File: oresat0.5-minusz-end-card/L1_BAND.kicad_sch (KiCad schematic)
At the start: 1 part

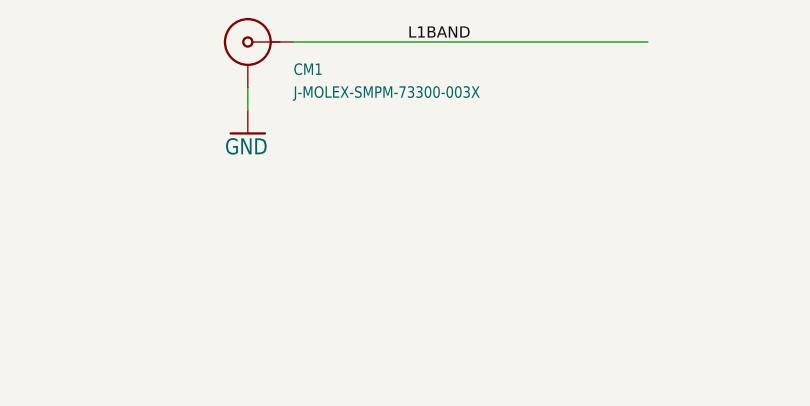
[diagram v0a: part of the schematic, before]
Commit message: Updated -Z end card and replaced eagle imported libraries with kicad libraries
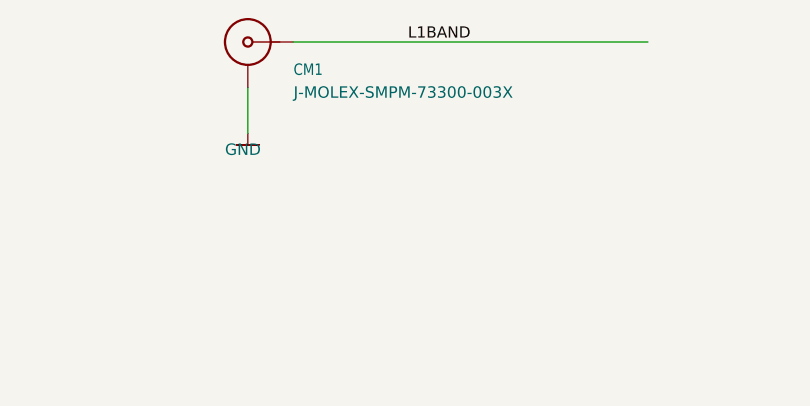
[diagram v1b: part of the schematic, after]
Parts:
- CM1: footprint oresat-footprints:J-MOLEX-SMPM-073300-003X -> oresat-connectors:J-MOLEX-SMPM-073300-003X; symbol OreSat-j-molex-smpm-73300-003x:J-MOLEX-SMPM-73300-003X -> oresat-connectors:J-MOLEX-SMPM-73300-003X
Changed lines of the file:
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@@
     (stroke (width 0) (type default) (color 0 0 0 0))
   )
-  (wire (pts (xy 57.15 139.7) (xy 57.15 137.16))
+  (wire (pts (xy 57.15 137.16) (xy 57.15 142.24))
     (stroke (width 0) (type default) (color 0 0 0 0))
   )
@@
     (effects (font (size 1.2446 1.2446)) (justify left bottom))
   )
-  (symbol (lib_id "OreSat-j-molex-smpm-73300-003x:J-MOLEX-SMPM-73300-003X") (at 57.15 132.08 0) (unit 1)
+  (symbol (lib_id "oresat-connectors:J-MOLEX-SMPM-73300-003X") (at 57.15 132.08 0) (unit 1)
     (in_bom yes) (on_board yes)
     (property "Reference" "CM1" (id 0) (at 62.23 135.89 0)
@@
     )
     (property "Value" "J-MOLEX-SMPM-73300-003X" (id 1) (at 62.23 138.43 0)
-      (effects (font (size 1.27 1.0795)) (justify left bottom))
+      (effects (font (size 1.27 1.27)) (justify left bottom))
     )
-    (property "Footprint" "oresat-footprints:J-MOLEX-SMPM-073300-003X" (id 2) (at 57.15 132.08 0)
+    (property "Footprint" "oresat-connectors:J-MOLEX-SMPM-073300-003X" (id 2) (at 57.15 132.08 0)
       (effects (font (size 1.27 1.27)) hide)
     )
@@
     (pin "RF")
   )
-  (symbol (lib_id "plusz-end-card-with-turnstile-eagle-import:GND") (at 57.15 142.24 0) (unit 1)
+  (symbol (lib_id "oresat-power:GND") (at 57.15 142.24 0) (unit 1)
     (in_bom yes) (on_board yes)
     (property "Reference" "#GND012" (id 0) (at 57.15 142.24 0)
@@
     )
     (property "Value" "GND" (id 1) (at 54.61 144.78 0)
-      (effects (font (size 1.778 1.5113)) (justify left bottom))
+      (effects (font (size 1.27 1.27)) (justify left bottom))
     )
     (property "Footprint" "plusz-end-card-with-turnstile:" (id 2) (at 57.15 142.24 0)

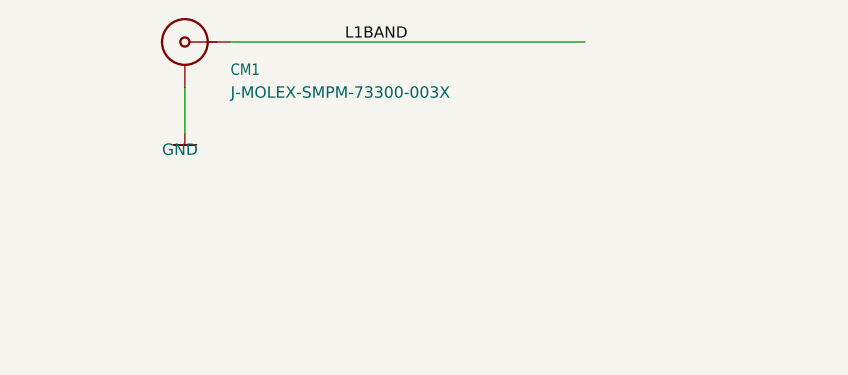
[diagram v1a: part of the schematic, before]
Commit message: -Z end card design review changes, and added antenna feeds
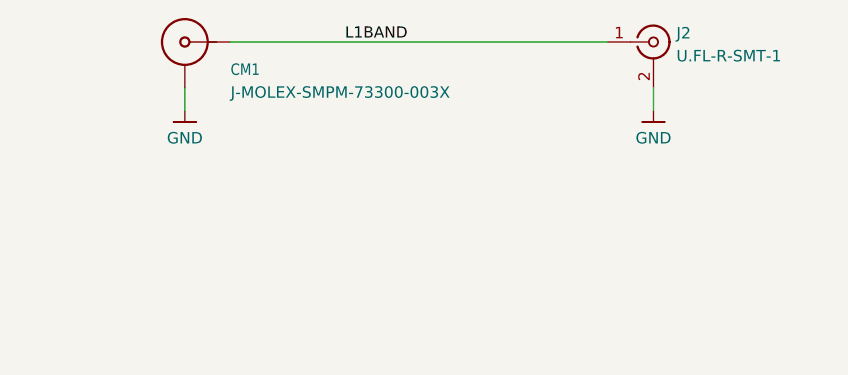
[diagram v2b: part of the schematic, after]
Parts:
- added J2: U.FL-R-SMT-1, Connector_Coaxial:U.FL_Hirose_U.FL-R-SMT-1_Vertical, symbol Connector:Conn_Coaxial
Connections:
- net GND: now also J2.2 (Ext)
- net L1BAND: now also J2.1 (In)
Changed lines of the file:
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@@
     (rev "1.0")
   )
-  (wire (pts (xy 62.23 132.08) (xy 101.6 132.08))
+  (wire (pts (xy 109.22 137.16) (xy 109.22 139.7))
     (stroke (width 0) (type default) (color 0 0 0 0))
   )
-  (wire (pts (xy 57.15 137.16) (xy 57.15 142.24))
+  (wire (pts (xy 62.23 132.08) (xy 104.14 132.08))
+    (stroke (width 0) (type default) (color 0 0 0 0))
+  )
+  (wire (pts (xy 57.15 137.16) (xy 57.15 139.7))
     (stroke (width 0) (type default) (color 0 0 0 0))
   )
@@
   (label "L1BAND" (at 74.93 132.08 0)
     (effects (font (size 1.2446 1.2446)) (justify left bottom))
+  )
+  (symbol (lib_id "Connector:Conn_Coaxial") (at 109.22 132.08 0) (unit 1)
+    (in_bom yes) (on_board yes) (fields_autoplaced)
+    (property "Reference" "J2" (id 0) (at 111.76 131.1031 0)
+      (effects (font (size 1.27 1.27)) (justify left))
+    )
+    (property "Value" "U.FL-R-SMT-1" (id 1) (at 111.76 133.6431 0)
+      (effects (font (size 1.27 1.27)) (justify left))
+    )
+    (property "Footprint" "Connector_Coaxial:U.FL_Hirose_U.FL-R-SMT-1_Vertical" (id 2) (at 109.22 132.08 0)
+      (effects (font (size 1.27 1.27)) hide)
+    )
+    (property "Datasheet" " ~" (id 3) (at 109.22 132.08 0)
+      (effects (font (size 1.27 1.27)) hide)
+    )
+    (pin "1")
+    (pin "2")
+  )
+  (symbol (lib_id "oresat-power:GND") (at 109.22 139.7 0) (unit 1)
+    (in_bom yes) (on_board yes)
+    (property "Reference" "#GND03" (id 0) (at 109.22 139.7 0)
+      (effects (font (size 1.27 1.27)) hide)
+    )
+    (property "Value" "GND" (id 1) (at 109.22 143.51 0)
+      (effects (font (size 1.27 1.27)) (justify bottom))
+    )
+    (property "Footprint" "plusz-end-card-with-turnstile:" (id 2) (at 109.22 139.7 0)
+      (effects (font (size 1.27 1.27)) hide)
+    )
+    (property "Datasheet" "" (id 3) (at 109.22 139.7 0)
+      (effects (font (size 1.27 1.27)) hide)
+    )
+    (pin "1")
   )
   (symbol (lib_id "oresat-connectors:J-MOLEX-SMPM-73300-003X") (at 57.15 132.08 0) (unit 1)
@@
     (pin "RF")
   )
-  (symbol (lib_id "oresat-power:GND") (at 57.15 142.24 0) (unit 1)
+  (symbol (lib_id "oresat-power:GND") (at 57.15 139.7 0) (unit 1)
     (in_bom yes) (on_board yes)
-    (property "Reference" "#GND012" (id 0) (at 57.15 142.24 0)
+    (property "Reference" "#GND012" (id 0) (at 57.15 139.7 0)
       (effects (font (size 1.27 1.27)) hide)
     )
-    (property "Value" "GND" (id 1) (at 54.61 144.78 0)
-      (effects (font (size 1.27 1.27)) (justify left bottom))
+    (property "Value" "GND" (id 1) (at 57.15 143.51 0)
+      (effects (font (size 1.27 1.27)) (justify bottom))
     )
-    (property "Footprint" "plusz-end-card-with-turnstile:" (id 2) (at 57.15 142.24 0)
+    (property "Footprint" "plusz-end-card-with-turnstile:" (id 2) (at 57.15 139.7 0)
       (effects (font (size 1.27 1.27)) hide)
     )
-    (property "Datasheet" "" (id 3) (at 57.15 142.24 0)
+    (property "Datasheet" "" (id 3) (at 57.15 139.7 0)
       (effects (font (size 1.27 1.27)) hide)
     )

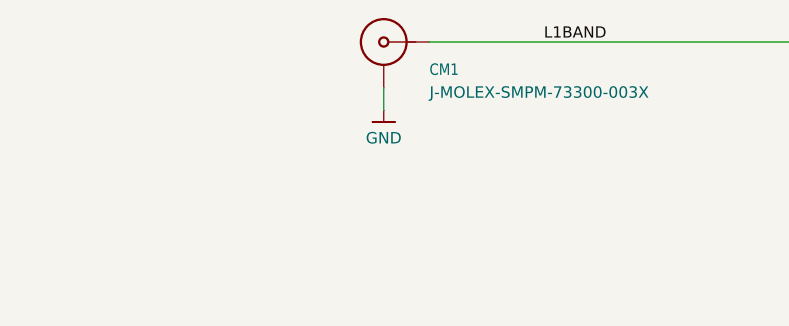
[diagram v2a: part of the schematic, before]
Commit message: Updated OreSat 0.5 end card board outlines and mounting holes, and fixed KiCad library warnings
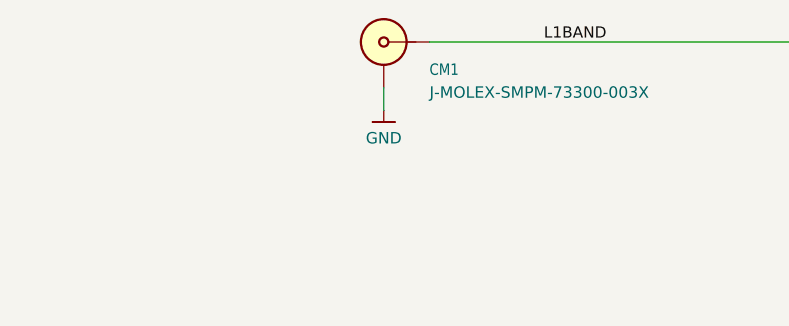
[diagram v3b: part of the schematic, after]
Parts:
- CM1: footprint oresat-connectors:J-MOLEX-SMPM-073300-003X -> oresat-connectors:J-MOLEX-SMPM-073300-002X; symbol oresat-connectors:J-MOLEX-SMPM-73300-003X -> oresat-connectors:J-MOLEX-SMPM-73300-002X
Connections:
- net GND: now also CM1.SHLD; no longer CM1.GND (SHIELD3)
- net L1BAND: now also CM1.SIG; no longer CM1.RF (CENTER)
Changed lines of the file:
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@@
-(kicad_sch (version 20211123) (generator eeschema)
+(kicad_sch (version 20230121) (generator eeschema)
   (paper "USLedger")
   (title_block
@@
   )
   (wire (pts (xy 109.22 137.16) (xy 109.22 139.7))
-    (stroke (width 0) (type default) (color 0 0 0 0))
+    (stroke (width 0) (type default))
   )
   (wire (pts (xy 62.23 132.08) (xy 104.14 132.08))
-    (stroke (width 0) (type default) (color 0 0 0 0))
+    (stroke (width 0) (type default))
   )
   (wire (pts (xy 57.15 137.16) (xy 57.15 139.7))
-    (stroke (width 0) (type default) (color 0 0 0 0))
+    (stroke (width 0) (type default))
   )
-  (text "L1 BAND Feed System (1.575 GHz)" (at 16.51 247.65 180)
+  (text "L1 BAND Feed System (1.575 GHz)" (at 16.51 247.65 0)
     (effects (font (size 4.064 3.4544)) (justify left bottom))
   )
-  (label "L1BAND" (at 74.93 132.08 0)
+  (label "L1BAND" (at 74.93 132.08 0) (fields_autoplaced)
     (effects (font (size 1.2446 1.2446)) (justify left bottom))
   )
   (symbol (lib_id "Connector:Conn_Coaxial") (at 109.22 132.08 0) (unit 1)
-    (in_bom yes) (on_board yes) (fields_autoplaced)
-    (property "Reference" "J2" (id 0) (at 111.76 131.1031 0)
+    (in_bom yes) (on_board yes) (dnp no) (fields_autoplaced)
+    (property "Reference" "J2" (at 111.76 131.1031 0)
       (effects (font (size 1.27 1.27)) (justify left))
     )
-    (property "Value" "U.FL-R-SMT-1" (id 1) (at 111.76 133.6431 0)
+    (property "Value" "U.FL-R-SMT-1" (at 111.76 133.6431 0)
       (effects (font (size 1.27 1.27)) (justify left))
     )
-    (property "Footprint" "Connector_Coaxial:U.FL_Hirose_U.FL-R-SMT-1_Vertical" (id 2) (at 109.22 132.08 0)
+    (property "Footprint" "Connector_Coaxial:U.FL_Hirose_U.FL-R-SMT-1_Vertical" (at 109.22 132.08 0)
       (effects (font (size 1.27 1.27)) hide)
     )
-    (property "Datasheet" " ~" (id 3) (at 109.22 132.08 0)
+    (property "Datasheet" " ~" (at 109.22 132.08 0)
       (effects (font (size 1.27 1.27)) hide)
     )
     (pin "1")
     (pin "2")
+    (instances
+      (project "oresat0.5-minusz-end-card"
+        (path "/f7595184-4323-4ed9-b19e-5e32e3c6e76f/c4a46bba-817b-433a-9d2e-3dc88315141d"
+          (reference "J2") (unit 1)
+        )
+      )
+    )
   )
   (symbol (lib_id "oresat-power:GND") (at 109.22 139.7 0) (unit 1)
-    (in_bom yes) (on_board yes)
-    (property "Reference" "#GND03" (id 0) (at 109.22 139.7 0)
+    (in_bom yes) (on_board yes) (dnp no)
+    (property "Reference" "#GND03" (at 109.22 139.7 0)
       (effects (font (size 1.27 1.27)) hide)
     )
-    (property "Value" "GND" (id 1) (at 109.22 143.51 0)
+    (property "Value" "GND" (at 109.22 143.51 0)
       (effects (font (size 1.27 1.27)) (justify bottom))
     )
-    (property "Footprint" "plusz-end-card-with-turnstile:" (id 2) (at 109.22 139.7 0)
+    (property "Footprint" "plusz-end-card-with-turnstile:" (at 109.22 139.7 0)
       (effects (font (size 1.27 1.27)) hide)
     )
-    (property "Datasheet" "" (id 3) (at 109.22 139.7 0)
+    (property "Datasheet" "" (at 109.22 139.7 0)
       (effects (font (size 1.27 1.27)) hide)
     )
     (pin "1")
+    (instances
+      (project "oresat0.5-minusz-end-card"
+        (path "/f7595184-4323-4ed9-b19e-5e32e3c6e76f/c4a46bba-817b-433a-9d2e-3dc88315141d"
+          (reference "#GND03") (unit 1)
+        )
+      )
+    )
   )
-  (symbol (lib_id "oresat-connectors:J-MOLEX-SMPM-73300-003X") (at 57.15 132.08 0) (unit 1)
-    (in_bom yes) (on_board yes)
-    (property "Reference" "CM1" (id 0) (at 62.23 135.89 0)
+  (symbol (lib_id "oresat-connectors:J-MOLEX-SMPM-73300-002X") (at 57.15 132.08 0) (unit 1)
+    (in_bom yes) (on_board yes) (dnp no)
+    (property "Reference" "CM1" (at 62.23 135.89 0)
       (effects (font (size 1.27 1.0795)) (justify left bottom))
     )
-    (property "Value" "J-MOLEX-SMPM-73300-003X" (id 1) (at 62.23 138.43 0)
+    (property "Value" "J-MOLEX-SMPM-73300-003X" (at 62.23 138.43 0)
       (effects (font (size 1.27 1.27)) (justify left bottom))
     )
-    (property "Footprint" "oresat-connectors:J-MOLEX-SMPM-073300-003X" (id 2) (at 57.15 132.08 0)
+    (property "Footprint" "oresat-connectors:J-MOLEX-SMPM-073300-002X" (at 57.15 125.73 0)
       (effects (font (size 1.27 1.27)) hide)
     )
-    (property "Datasheet" "" (id 3) (at 57.15 132.08 0)
+    (property "Datasheet" "https://tools.molex.com/pdm_docs/sd/733000020_sd.pdf" (at 57.15 123.19 0)
       (effects (font (size 1.27 1.27)) hide)
     )
-    (pin "GND")
-    (pin "RF")
+    (pin "SHLD")
+    (pin "SIG")
+    (instances
+      (project "oresat0.5-minusz-end-card"
+        (path "/f7595184-4323-4ed9-b19e-5e32e3c6e76f/c4a46bba-817b-433a-9d2e-3dc88315141d"
+          (reference "CM1") (unit 1)
+        )
+      )
+    )
   )
   (symbol (lib_id "oresat-power:GND") (at 57.15 139.7 0) (unit 1)
-    (in_bom yes) (on_board yes)
-    (property "Reference" "#GND012" (id 0) (at 57.15 139.7 0)
+    (in_bom yes) (on_board yes) (dnp no)
+    (property "Reference" "#GND012" (at 57.15 139.7 0)
       (effects (font (size 1.27 1.27)) hide)
     )
-    (property "Value" "GND" (id 1) (at 57.15 143.51 0)
+    (property "Value" "GND" (at 57.15 143.51 0)
       (effects (font (size 1.27 1.27)) (justify bottom))
     )
-    (property "Footprint" "plusz-end-card-with-turnstile:" (id 2) (at 57.15 139.7 0)
+    (property "Footprint" "plusz-end-card-with-turnstile:" (at 57.15 139.7 0)
       (effects (font (size 1.27 1.27)) hide)
     )
-    (property "Datasheet" "" (id 3) (at 57.15 139.7 0)
+    (property "Datasheet" "" (at 57.15 139.7 0)
       (effects (font (size 1.27 1.27)) hide)
     )
     (pin "1")
+    (instances
+      (project "oresat0.5-minusz-end-card"
+        (path "/f7595184-4323-4ed9-b19e-5e32e3c6e76f/c4a46bba-817b-433a-9d2e-3dc88315141d"
+          (reference "#GND012") (unit 1)
+        )
+      )
+    )
   )
 )
